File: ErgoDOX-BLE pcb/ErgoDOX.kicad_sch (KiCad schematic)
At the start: 109 parts, among them J1 Conn_01x04, J2 Conn_01x02_Female, J4 Conn_01x02, J5 Conn_01x02, J6 6PIN, P1 USB_C_Plug_USB2.0, Q1 Q_NPN_BCE, SW0:10 SW0:3, SW0:11 SW0:2, SW0:12 SW0:1, SW0:7 SW0:6, SW0:8 SW0:5, SW0:9 SW0:4, SW1:10 SW1:3, SW1:11 SW1:2, SW1:12 SW1:1, SW1:13 SW1:0, SW1:9 SW1:4, SW2:10 SW2:3, SW2:11 SW2:2, SW2:12 SW2:1, SW2:13 SW2:0, SW2:7 SW2:6, SW2:8 SW2:5, SW2:9 SW2:4, SW3:10 SW3:3, SW3:11 SW3:2, SW3:12 SW3:1, SW3:13 SW3:0, SW3:8 SW3:5, SW3:9 SW3:4, SW4:10 SW4:3, SW4:11 SW4:2, SW4:12 SW4:1, SW4:13 SW4:0, SW4:7 SW4:6, SW4:8 SW4:5, SW4:9 SW4:4, SW5:10 SW5:3, SW5:11 SW5:2, SW5:12 SW5:1, SW5:13 SW5:0, SW5:7 SW5:6, SW5:8 SW5:5, SW5:9 SW5:4, U1 MCP23018, U2 MCP73831-2-OT

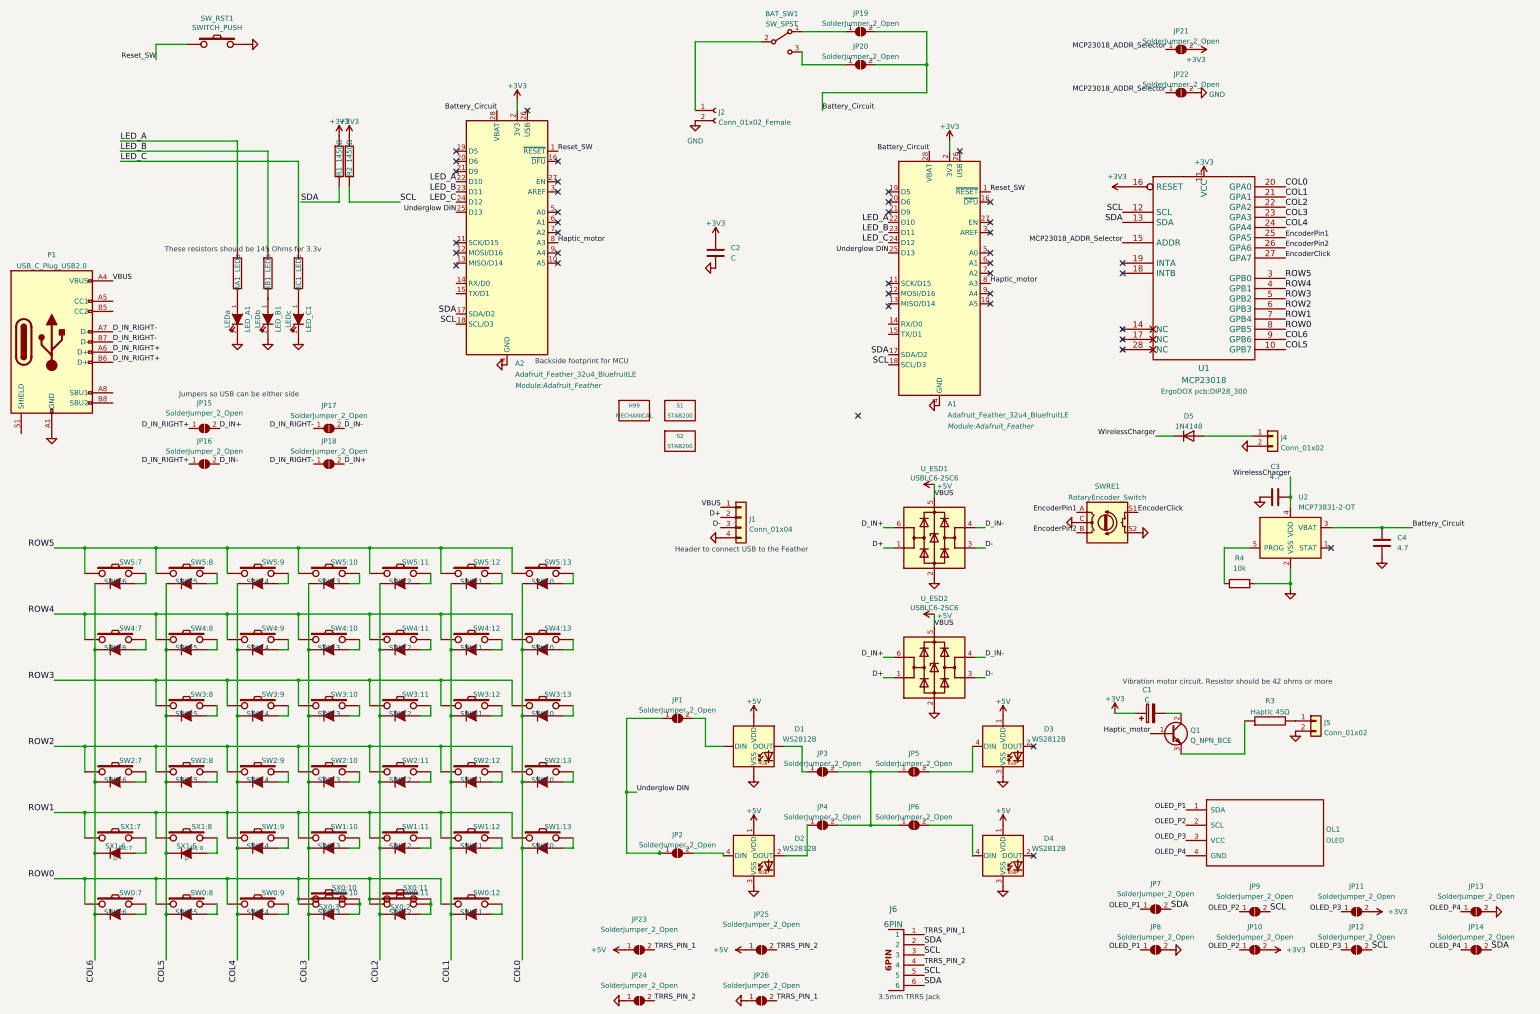
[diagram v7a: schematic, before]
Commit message: Add 3v3 regulator
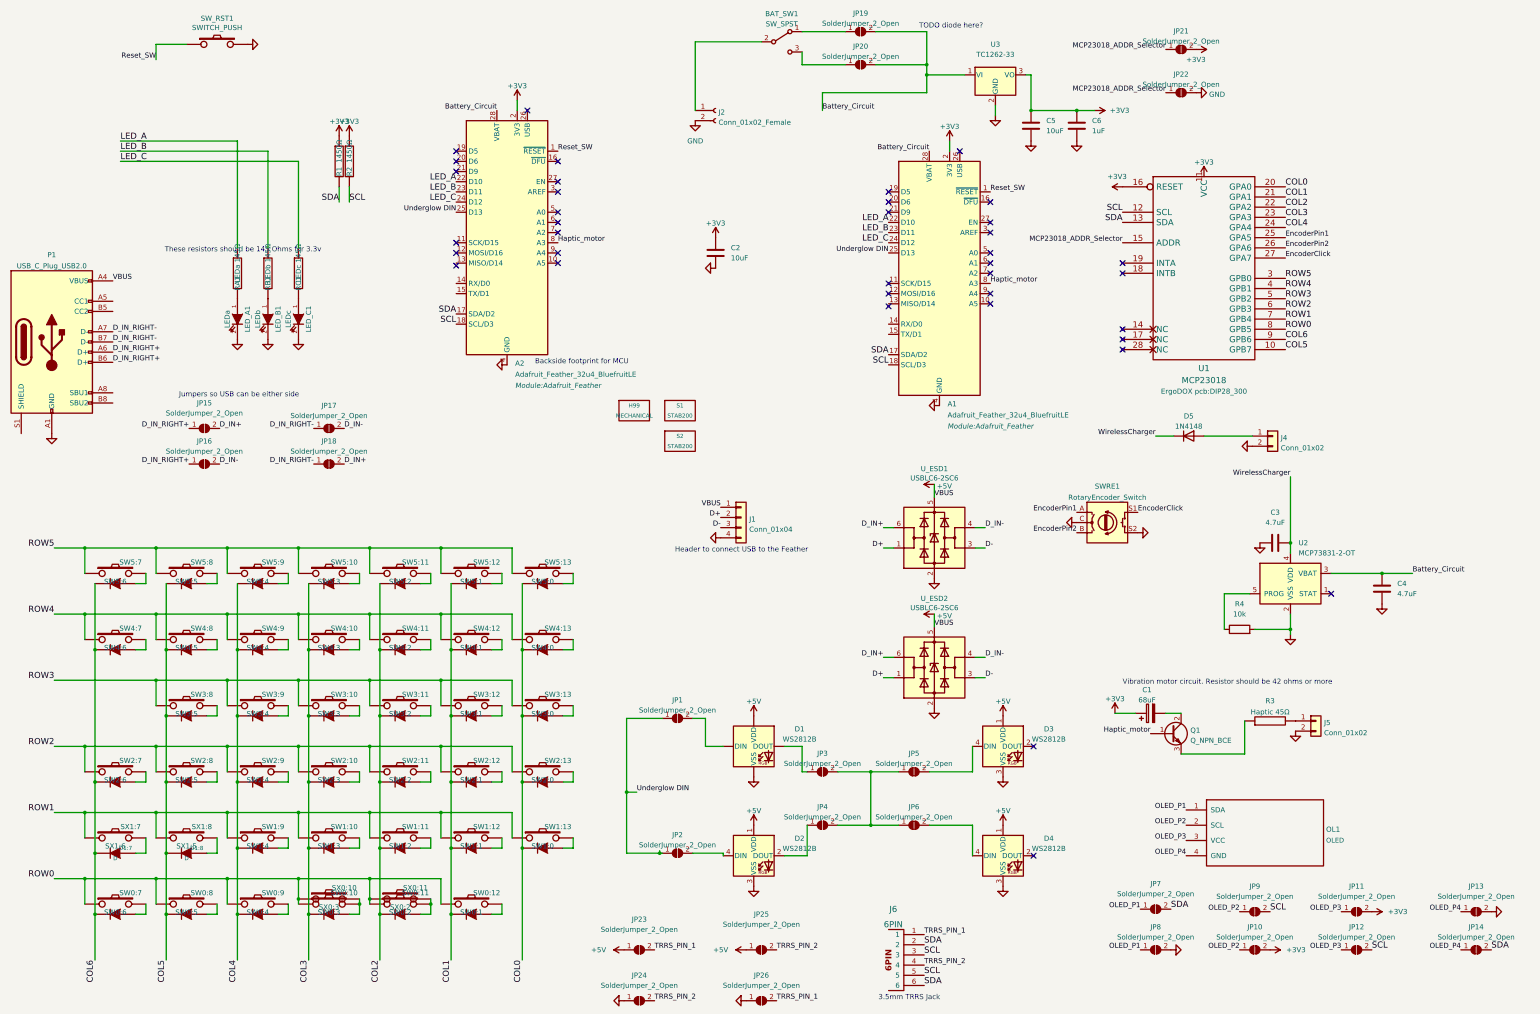
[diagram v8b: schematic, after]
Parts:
- added C5: 10uF, symbol Device:C
- added C6: 1uF, symbol Device:C
- added U3: TC1262-33, Package_TO_SOT_THT:TO-220-3_Vertical, symbol Regulator_Linear:TC1262-33
- C1: value C -> 68uF
- C2: value C -> 10uF
- C3, C4: value 4.7 -> 4.7uF
- RA1: value LEDa -> LEDa 145Ω
- RB1: value LEDb -> LEDb 145Ω
- RC1: value LEDc -> LEDc 145Ω
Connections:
- net +3V3: now also C5.1, C6.1, U3.3 (VO)
- net Battery_Circuit: now also U3.1 (VI)
- net GND: now also C5.2, C6.2, U3.2 (GND)
- no-connect marks 39 -> 38
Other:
- note added: "TODO diode here?"
- moved on the sheet: C3, C4, R4, U2
